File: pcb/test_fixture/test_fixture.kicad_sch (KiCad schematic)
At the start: 43 parts, among them J1 UART, J2 Power Input, J3 Conn_ARM_JTAG_SWD_10, J5 GND, J6 GND, P3.3V1 

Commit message: [pcb] finalized the fixture
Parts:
- added H10, H8, H9: Stand Mount, MountingHole:MountingHole_2.1mm, symbol Mechanical:MountingHole
- added H7: (no value), symbol Mechanical:MountingHole
- added POGO19: pogo, dictofun:POGO_PIN, symbol Connector:Conn_01x01_Female
- H1: value (none) -> PCB Mount; footprint (none) -> MountingHole:MountingHole_2.1mm
- H2: value (none) -> PCB Mount
- H3: value (none) -> Outer PCB Mount
- J4: footprint (none) -> Connector_PinSocket_2.54mm:PinSocket_1x01_P2.54mm_Vertical
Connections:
- new net CHRG_IN: POGO19.1 (Pin_1)
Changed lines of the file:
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@@
   (junction (at 110.49 132.08) (diameter 0) (color 0 0 0 0)
   )
+  (wire (pts (xy 99.06 153.67) (xy 110.49 153.67))
+    (stroke (width 0) (type default) (color 0 0 0 0))
+  )
   (wire (pts (xy 99.06 113.03) (xy 110.49 113.03))
     (stroke (width 0) (type default) (color 0 0 0 0))
@@
   )
   (label "SPI_CLK" (at 100.33 102.87 0)
+    (effects (font (size 1.27 1.27)) (justify left bottom))
+  )
+  (label "CHRG_IN" (at 99.06 153.67 0)
     (effects (font (size 1.27 1.27)) (justify left bottom))
   )
@@
     )
     (property "Value" "" (id 1) (at 132.08 65.405 90)
-      (effects (font (size 1.27 1.27)) (justify right))
-    )
-    (property "Footprint" "" (id 2) (at 133.985 66.675 0)
+      (effects (font (size 1.27 1.27)) (justify right) hide)
+    )
+    (property "Footprint" "Connector_PinSocket_2.54mm:PinSocket_1x01_P2.54mm_Vertical" (id 2) (at 133.985 66.675 0)
       (effects (font (size 1.27 1.27)) hide)
     )
@@
     (pin "1")
   )
+  (symbol (lib_id "Mechanical:MountingHole") (at 172.085 76.2 0) (unit 1)
+    (in_bom yes) (on_board yes) (fields_autoplaced)
+    (property "Reference" "H7" (id 0) (at 175.26 74.9299 0)
+      (effects (font (size 1.27 1.27)) (justify left))
+    )
+    (property "Value" "" (id 1) (at 175.26 77.4699 0)
+      (effects (font (size 1.27 1.27)) (justify left))
+    )
+    (property "Footprint" "" (id 2) (at 172.085 76.2 0)
+      (effects (font (size 1.27 1.27)) hide)
+    )
+    (property "Datasheet" "~" (id 3) (at 172.085 76.2 0)
+      (effects (font (size 1.27 1.27)) hide)
+    )
+  )
   (symbol (lib_id "Connector:TestPoint") (at 99.06 113.03 90) (unit 1)
     (in_bom yes) (on_board yes)
@@
       (effects (font (size 1.27 1.27)) (justify left))
     )
-    (property "Value" "" (id 1) (at 175.26 43.8149 0)
+    (property "Value" "Outer PCB Mount" (id 1) (at 175.26 43.8149 0)
       (effects (font (size 1.27 1.27)) (justify left))
     )
@@
     (pin "9")
   )
+  (symbol (lib_id "Mechanical:MountingHole") (at 172.085 91.44 0) (unit 1)
+    (in_bom yes) (on_board yes) (fields_autoplaced)
+    (property "Reference" "H10" (id 0) (at 175.26 90.1699 0)
+      (effects (font (size 1.27 1.27)) (justify left))
+    )
+    (property "Value" "Stand Mount" (id 1) (at 175.26 92.7099 0)
+      (effects (font (size 1.27 1.27)) (justify left))
+    )
+    (property "Footprint" "MountingHole:MountingHole_2.1mm" (id 2) (at 172.085 91.44 0)
+      (effects (font (size 1.27 1.27)) hide)
+    )
+    (property "Datasheet" "~" (id 3) (at 172.085 91.44 0)
+      (effects (font (size 1.27 1.27)) hide)
+    )
+  )
   (symbol (lib_id "Connector:Conn_01x01_Female") (at 126.365 52.07 0) (unit 1)
     (in_bom yes) (on_board yes) (fields_autoplaced)
@@
     (in_bom yes) (on_board yes)
     (property "Reference" "J6" (id 0) (at 143.51 62.865 90)
-      (effects (font (size 1.27 1.27)) (justify right))
+      (effects (font (size 1.27 1.27)) (justify right) hide)
     )
     (property "Value" "GND" (id 1) (at 142.24 65.405 90)
@@
     (pin "1")
   )
+  (symbol (lib_id "Mechanical:MountingHole") (at 172.085 86.36 0) (unit 1)
+    (in_bom yes) (on_board yes) (fields_autoplaced)
+    (property "Reference" "H9" (id 0) (at 175.26 85.0899 0)
+      (effects (font (size 1.27 1.27)) (justify left))
+    )
+    (property "Value" "Stand Mount" (id 1) (at 175.26 87.6299 0)
+      (effects (font (size 1.27 1.27)) (justify left))
+    )
+    (property "Footprint" "MountingHole:MountingHole_2.1mm" (id 2) (at 172.085 86.36 0)
+      (effects (font (size 1.27 1.27)) hide)
+    )
+    (property "Datasheet" "~" (id 3) (at 172.085 86.36 0)
+      (effects (font (size 1.27 1.27)) hide)
+    )
+  )
   (symbol (lib_id "Mechanical:MountingHole") (at 148.59 43.18 0) (unit 1)
     (in_bom yes) (on_board yes) (fields_autoplaced)
@@
       (effects (font (size 1.27 1.27)) (justify left))
     )
-    (property "Value" "" (id 1) (at 151.13 44.4499 0)
-      (effects (font (size 1.27 1.27)) (justify left))
-    )
-    (property "Footprint" "" (id 2) (at 148.59 43.18 0)
+    (property "Value" "PCB Mount" (id 1) (at 151.13 44.4499 0)
+      (effects (font (size 1.27 1.27)) (justify left))
+    )
+    (property "Footprint" "MountingHole:MountingHole_2.1mm" (id 2) (at 148.59 43.18 0)
       (effects (font (size 1.27 1.27)) hide)
     )
@@
     )
     (pin "1")
+  )
+  (symbol (lib_id "Mechanical:MountingHole") (at 172.085 81.28 0) (unit 1)
+    (in_bom yes) (on_board yes) (fields_autoplaced)
+    (property "Reference" "H8" (id 0) (at 175.26 80.0099 0)
+      (effects (font (size 1.27 1.27)) (justify left))
+    )
+    (property "Value" "Stand Mount" (id 1) (at 175.26 82.5499 0)
+      (effects (font (size 1.27 1.27)) (justify left))
+    )
+    (property "Footprint" "MountingHole:MountingHole_2.1mm" (id 2) (at 172.085 81.28 0)
+      (effects (font (size 1.27 1.27)) hide)
+    )
+    (property "Datasheet" "~" (id 3) (at 172.085 81.28 0)
+      (effects (font (size 1.27 1.27)) hide)
+    )
   )
   (symbol (lib_id "Connector:TestPoint") (at 99.06 102.87 90) (unit 1)
@@
       (effects (font (size 1.27 1.27)) (justify left))
     )
-    (property "Value" "" (id 1) (at 151.13 50.1649 0)
+    (property "Value" "PCB Mount" (id 1) (at 151.13 50.1649 0)
       (effects (font (size 1.27 1.27)) (justify left))
     )
@@
     (pin "1")
   )
+  (symbol (lib_id "Connector:Conn_01x01_Female") (at 115.57 153.67 0) (unit 1)
+    (in_bom yes) (on_board yes) (fields_autoplaced)
+    (property "Reference" "POGO19" (id 0) (at 116.84 153.6699 0)
+      (effects (font (size 1.27 1.27)) (justify left))
+    )
+    (property "Value" "pogo" (id 1) (at 117.475 154.9399 0)
+      (effects (font (size 1.27 1.27)) (justify left) hide)
+    )
+    (property "Footprint" "dictofun:POGO_PIN" (id 2) (at 115.57 153.67 0)
+      (effects (font (size 1.27 1.27)) hide)
+    )
+    (property "Datasheet" "https://www.digikey.de/de/products/detail/mill-max-manufacturing-corp/0985-1-15-20-71-14-11-0/5823029" (id 3) (at 115.57 153.67 0)
+      (effects (font (size 1.27 1.27)) hide)
+    )
+    (pin "1")
+  )
   (symbol (lib_id "Connector:Conn_01x01_Female") (at 109.22 31.75 0) (unit 1)
     (in_bom yes) (on_board yes) (fields_autoplaced)
@@
     (in_bom yes) (on_board yes)
     (property "Reference" "J5" (id 0) (at 138.43 62.865 90)
-      (effects (font (size 1.27 1.27)) (justify right))
+      (effects (font (size 1.27 1.27)) (justify right) hide)
     )
     (property "Value" "GND" (id 1) (at 137.16 65.405 90)
@@
       (reference "H6") (unit 1) (value "Outer PCB Mount") (footprint "MountingHole:MountingHole_2.1mm")
     )
+    (path "/1c7cee09-d75c-450e-81db-90dbec975075"
+      (reference "H7") (unit 1) (value "Stand Mount") (footprint "MountingHole:MountingHole_2.1mm")
+    )
+    (path "/cadfbee1-5938-40e2-a73c-24d10b84176d"
+      (reference "H8") (unit 1) (value "Stand Mount") (footprint "MountingHole:MountingHole_2.1mm")
+    )
+    (path "/bfbb6f2d-8021-42ec-acb0-5173112ac375"
+      (reference "H9") (unit 1) (value "Stand Mount") (footprint "MountingHole:MountingHole_2.1mm")
+    )
+    (path "/357e256b-c67e-4456-9af3-4ef77ef31b91"
+      (reference "H10") (unit 1) (value "Stand Mount") (footprint "MountingHole:MountingHole_2.1mm")
+    )
     (path "/04dfc243-0f51-4603-bf53-e1e3c0de09b3"
       (reference "J1") (unit 1) (value "UART") (footprint "Connector_PinHeader_2.54mm:PinHeader_1x03_P2.54mm_Vertical")
@@
       (reference "POGO18") (unit 1) (value "pogo") (footprint "dictofun:POGO_PIN")
     )
+    (path "/d6a7f71a-4da6-4997-9a3d-af77c0308253"
+      (reference "POGO19") (unit 1) (value "pogo") (footprint "dictofun:POGO_PIN")
+    )
     (path "/ab6ada93-7d78-4a48-9ca8-f6276f0f8575"

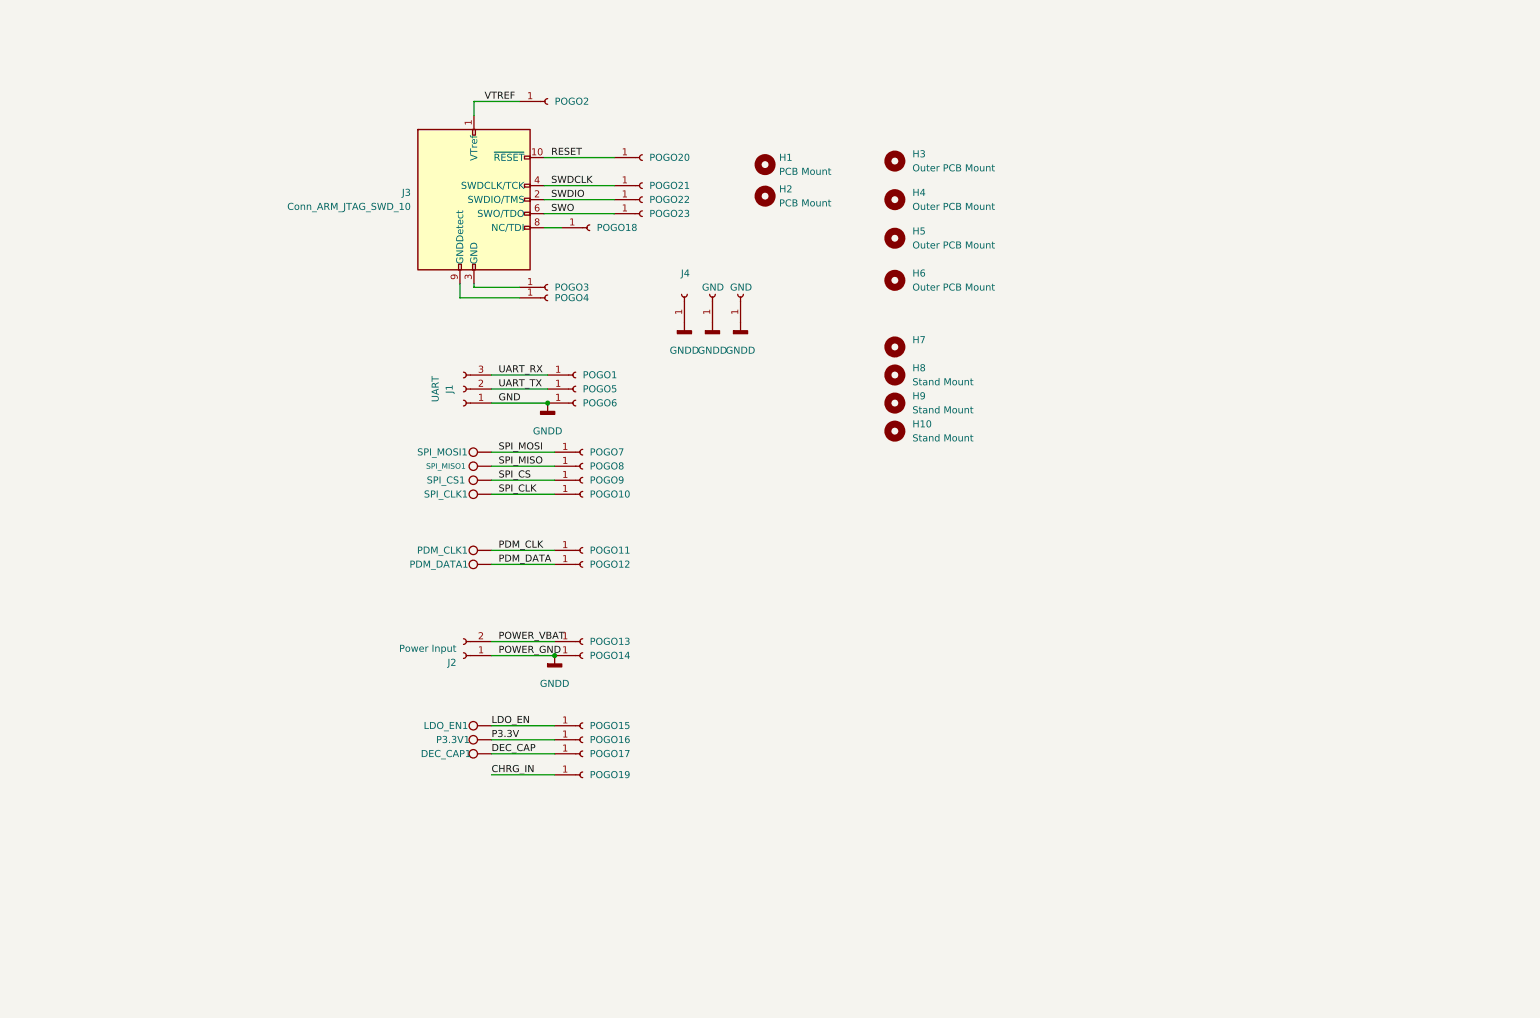
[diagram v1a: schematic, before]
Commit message: [pcb] version 1.3 (#75)
Changes:
    LDO voltage regulator replaced with DC-DC (expected increase in efficiency)
    added small-footprint RTC chip
    analog latch for regulator EN pin replaced with a digital flip-flop

Fixture:
    added Raspberry Pico to the PCB
    added current measurement setup
    planning to reduce hardware in use to a single PCB
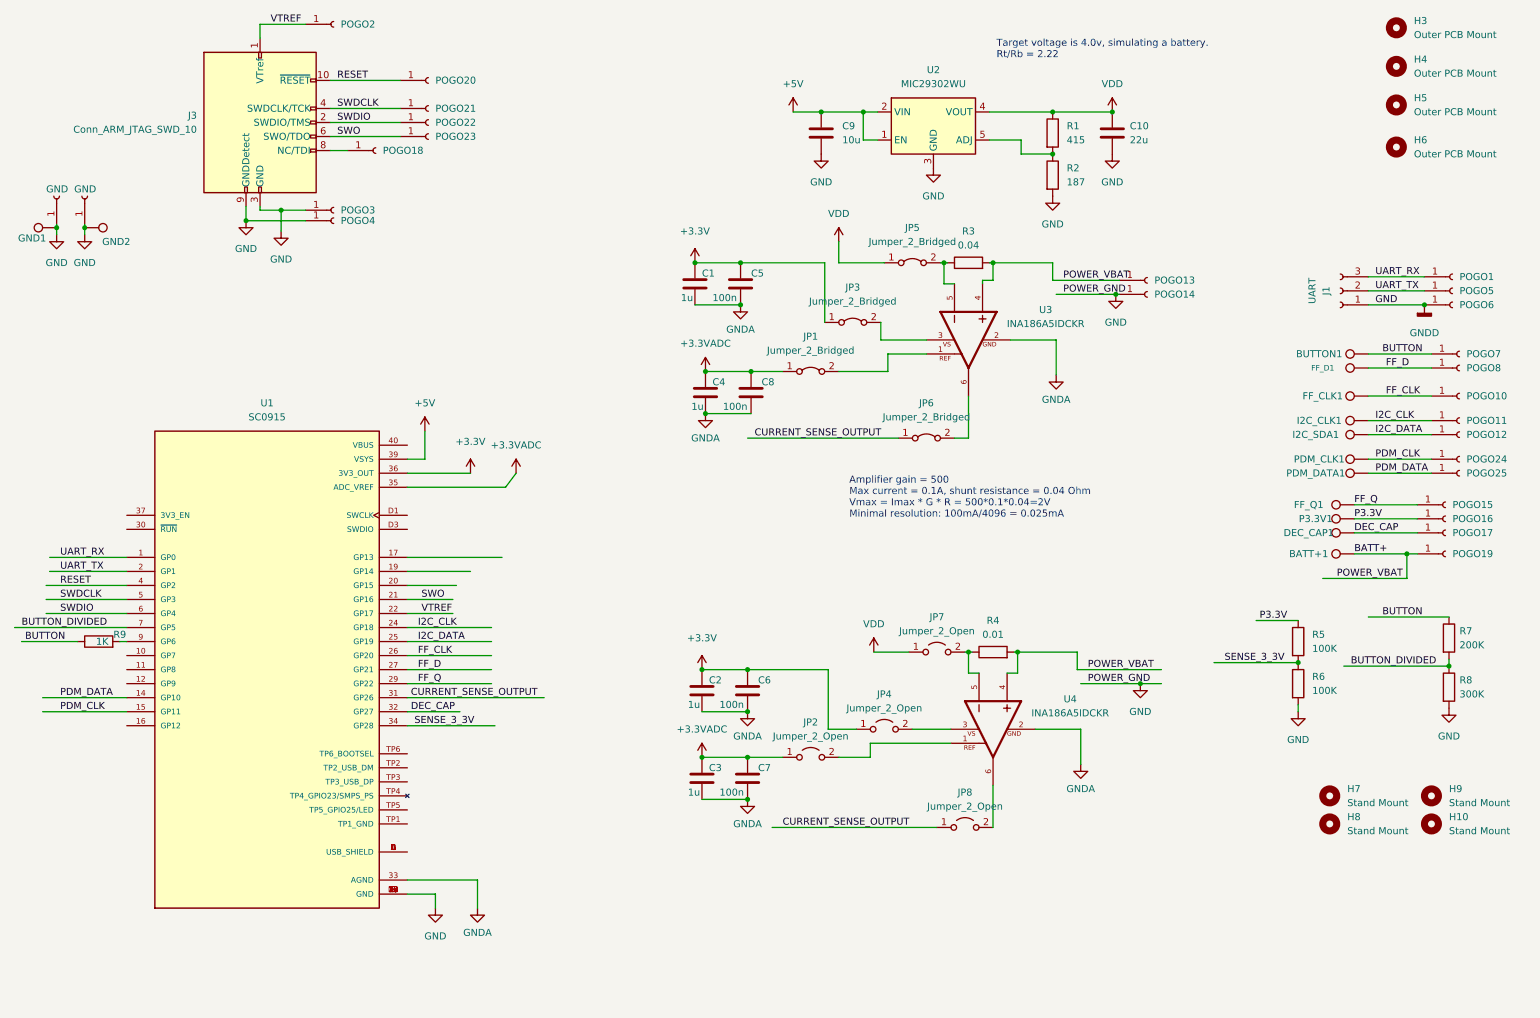
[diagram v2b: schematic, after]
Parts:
- removed H1, H2: PCB Mount, MountingHole:MountingHole_2.1mm, symbol Mechanical:MountingHole
- removed J2: Power Input, Connector_PinHeader_2.54mm:PinHeader_1x02_P2.54mm_Vertical, symbol Connector:Conn_01x02_Female
- removed J4: (no value), Connector_PinSocket_2.54mm:PinSocket_1x01_P2.54mm_Vertical, symbol Connector:Conn_01x01_Female
- removed POGO9: pogo, dictofun:POGO_PIN, symbol Connector:Conn_01x01_Female
- removed SPI_CS1: (no value), TestPoint:TestPoint_Pad_D1.5mm, symbol Connector:TestPoint
- added BATT+1, GND1, GND2, PDM_CLK1, PDM_DATA1: (no value), TestPoint:TestPoint_Pad_D1.5mm, symbol Connector:TestPoint
- added C1, C2, C3, C4: 1u, Resistor_SMD:R_1206_3216Metric, symbol Device:C
- added C10: 22u, Capacitor_SMD:C_1206_3216Metric, symbol Device:C
- added C5, C6, C7, C8: 100n, Resistor_SMD:R_1206_3216Metric, symbol Device:C
- added C9: 10u, Resistor_SMD:R_1206_3216Metric, symbol Device:C
- added JP1, JP3, JP5, JP6: Jumper_2_Bridged, Jumper:SolderJumper-2_P1.3mm_Bridged2Bar_Pad1.0x1.5mm, symbol Jumper:Jumper_2_Bridged
- added JP2, JP4, JP7, JP8: Jumper_2_Open, Jumper:SolderJumper-2_P1.3mm_Open_RoundedPad1.0x1.5mm, symbol Jumper:Jumper_2_Open
- added POGO24, POGO25: pogo, fixture:POGO, symbol Connector:Conn_01x01_Female
- added R1: 415, Resistor_SMD:R_0603_1608Metric, symbol Device:R
- added R2: 187, Resistor_SMD:R_0603_1608Metric, symbol Device:R
- added R3: 0.04, Resistor_SMD:R_Shunt_Vishay_WSR2_WSR3_KelvinConnection, symbol Device:R
- added R4: 0.01, Resistor_SMD:R_Shunt_Vishay_WSR2_WSR3_KelvinConnection, symbol Device:R
- added R5, R6: 100K, Resistor_SMD:R_0603_1608Metric, symbol Device:R
- added R7: 200K, Resistor_SMD:R_0603_1608Metric, symbol Device:R
- added R8: 300K, Resistor_SMD:R_0603_1608Metric, symbol Device:R
- added R9: 1K, Resistor_SMD:R_0603_1608Metric, symbol Device:R
- added U1: SC0915, MODULE_SC0915, symbol fixture:SC0915
- added U2: MIC29302WU, Package_TO_SOT_SMD:TO-263-5_TabPin3, symbol Regulator_Linear:MIC29302WU
- added U3, U4: INA186A5IDCKR, SOT65P210X110-6N, symbol fixture:INA186A1IDCKR
- H7: value (none) -> Stand Mount; footprint (none) -> MountingHole:MountingHole_2.1mm
- J5, J6: footprint Connector_PinSocket_2.54mm:PinSocket_1x01_P2.54mm_Vertical -> fixture:POGO
- POGO1, POGO10, POGO11, POGO12, POGO13, POGO14, POGO15, POGO16, POGO17, POGO18, POGO19, POGO2, POGO20, POGO21, POGO22, POGO23, POGO3, POGO4, POGO5, POGO6, POGO7, POGO8: footprint dictofun:POGO_PIN -> fixture:POGO
- renumbered SPI_MOSI1 to BUTTON1, SPI_CLK1 to FF_CLK1, SPI_MISO1 to FF_D1, LDO_EN1 to FF_Q1, PDM_CLK1 to I2C_CLK1, PDM_DATA1 to I2C_SDA1
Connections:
- net GNDD is gone; now on net GND: J1.1 (Pin_1), J5.1 (Pin_1), J6.1 (Pin_1), POGO14.1 (Pin_1), POGO6.1 (Pin_1)
- net POWER_VBAT is gone; now on net BATT+: POGO13.1 (Pin_1)
- net DEC_CAP: now also U1.32 (GP27)
- net P3.3V: now also R5.1
- net PDM_CLK: now also PDM_CLK1.1, POGO24.1 (Pin_1), U1.15 (GP11); no longer I2C_CLK1.1, POGO11.1 (Pin_1)
- net PDM_DATA: now also PDM_DATA1.1, POGO25.1 (Pin_1), U1.14 (GP10); no longer I2C_SDA1.1, POGO12.1 (Pin_1)
- net RESET: now also U1.4 (GP2)
- net SWDCLK: now also U1.5 (GP3)
- net SWDIO: now also U1.6 (GP4)
- net SWO: now also U1.21 (GP16)
- net UART_RX: now also U1.1 (GP0)
- net UART_TX: now also U1.2 (GP1)
- net VTREF: now also U1.22 (GP17)
- net GND: now reaches J3.3 (GND), J3.5 (GND), POGO3.1 (Pin_1)
- net GND: now also J3.9 (GNDDetect), POGO4.1 (Pin_1), C10.2, C9.2, GND1.1, GND2.1, R2.2, R6.2, R8.2, U1.13 (GND), U1.18 (GND), U1.23 (GND), U1.28 (GND), U1.3 (GND), U1.38 (GND), U1.8 (GND), U1.D2 (GND), U2.3 (GND)
- net CHRG_IN renamed BATT+
- net BATT+: now also BATT+1.1, R3.2, R4.2, U3.4, U4.4
- net LDO_EN renamed FF_Q
- net FF_Q: now also U1.29 (GP22)
- net SPI_CLK renamed FF_CLK
- net FF_CLK: now also U1.26 (GP20)
- net SPI_MISO renamed FF_D
- net FF_D: now also U1.27 (GP21)
- net SPI_MOSI renamed BUTTON
- net BUTTON: now also R7.1, R9.1
- new net: JP2.2 (B), U4.1
- new net: JP4.2 (B), U4.3
- new net: JP7.2 (B), R4.1, U4.5
- new net: JP8.2 (B), U4.6
- new net: JP5.2 (B), R3.1, U3.5
- new net: JP1.2 (B), U3.1
- new net: R1.2, R2.1, U2.5 (ADJ)
- new net: R9.2, U1.9 (GP6)
- new net: U1.A (USB_SHIELD), U1.B (USB_SHIELD), U1.C (USB_SHIELD), U1.D (USB_SHIELD)
- new net: JP3.2 (B), U3.3
- new net: JP6.2 (B), U3.6
- new net +3.3V: C1.1, C2.1, C5.1, C6.1, JP3.1 (A), JP4.1 (A), U1.36 (3V3_OUT)
- new net +3.3VADC: C3.1, C4.1, C7.1, C8.1, JP1.1 (A), JP2.1 (A), U1.35 (ADC_VREF)
- new net +5V: C9.1, U1.39 (VSYS), U2.1 (EN), U2.2 (VIN)
- new net BUTTON_DIVIDED: R7.2, R8.1, U1.7 (GP5)
- new net CURRENT_SENSE_OUTPUT: JP6.1 (A), JP8.1 (A), U1.31 (GP26)
- new net GNDA: C1.2, C2.2, C3.2, C4.2, C5.2, C6.2, C7.2, C8.2, U1.33 (AGND), U3.2, U4.2
- new net I2C_CLK: I2C_CLK1.1, POGO11.1 (Pin_1), U1.24 (GP18)
- new net I2C_DATA: I2C_SDA1.1, POGO12.1 (Pin_1), U1.25 (GP19)
- new net SENSE_3_3V: R5.2, R6.1, U1.34 (GP28)
- new net VDD: C10.1, JP5.1 (A), JP7.1 (A), R1.1, U2.4 (VOUT)
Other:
- note added: "Amplifier gain = 500 Max current = 0.1A, shunt resistance = 0.04 Ohm Vmax = Imax * G * R = 500*0.1*0.04=2V Minimal resolution: 100mA/4096 = 0.025mA"
- note added: "Target voltage is 4.0v, simulating a battery. Rt/Rb = 2.22"
- moved on the sheet: BUTTON1, DEC_CAP1, FF_CLK1, FF_D1, FF_Q1, H10, H3, H4, H5, H6, H7, H8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

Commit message: PCB v1.4 (#175)
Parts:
- removed C2, C3: 1u, Resistor_SMD:R_1206_3216Metric, symbol Device:C
- removed C6, C7: 100n, Resistor_SMD:R_1206_3216Metric, symbol Device:C
- removed DEC_CAP1, GND1, GND2, PDM_CLK1, PDM_DATA1: (no value), TestPoint:TestPoint_Pad_D1.5mm, symbol Connector:TestPoint
- removed J5, J6: GND, fixture:POGO, symbol Connector:Conn_01x01_Female
- removed JP1, JP3, JP5, JP6: Jumper_2_Bridged, Jumper:SolderJumper-2_P1.3mm_Bridged2Bar_Pad1.0x1.5mm, symbol Jumper:Jumper_2_Bridged
- removed JP2, JP4, JP7, JP8: Jumper_2_Open, Jumper:SolderJumper-2_P1.3mm_Open_RoundedPad1.0x1.5mm, symbol Jumper:Jumper_2_Open
- removed POGO17, POGO18, POGO20, POGO23, POGO24, POGO25, POGO4: pogo, fixture:POGO, symbol Connector:Conn_01x01_Female
- removed U4: INA186A5IDCKR, SOT65P210X110-6N, symbol fixture:INA186A1IDCKR
- added Q1: NMOS, Package_TO_SOT_SMD:SOT-23, symbol Simulation_SPICE:NMOS
- added R10: 1K, Resistor_SMD:R_0603_1608Metric, symbol Device:R
- R4: value 0.01 -> 100K; footprint Resistor_SMD:R_Shunt_Vishay_WSR2_WSR3_KelvinConnection -> Resistor_SMD:R_0603_1608Metric; LCSC C499494 -> C122538
- renumbered P3.3V1 to VCC_SENSE1
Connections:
- net +3.3V: now also U3.3
- net +3.3VADC: now also U3.1
- net BATT+: no longer R4.2
- net BUTTON: now also Q1.3 (S); no longer R9.1
- net CURRENT_SENSE_OUTPUT: now also U3.6
- net GND: now also R4.2; no longer J3.9 (GNDDetect)
- net RESET: no longer J3.10 (~{RESET})
- net SENSE_3_3V: no longer R5.2, R6.1
- net SWO: no longer J3.6 (SWO/TDO)
- net VDD: now also R3.1, U3.5, Q1.1 (D)
- net BUTTON_CTRL: now reaches R4.1
- net BUTTON_CTRL: now also R9.1, R10.1
- net DEC_CAP: no longer names the net of U1.32 (GP27)
- net P3.3V renamed P1.9V
- net P1.9V: no longer R5.1
- new net: Q1.2 (G), R10.2
- new net SENSE_VCC: R5.2, R6.1
- new net VCC_SENSE1: R5.1
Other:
- note added: "TODO: add a level-shifter on the UART towards DUT"
